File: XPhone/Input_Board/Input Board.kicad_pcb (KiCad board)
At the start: 2 copper layers, 100 x 100 mm, 94 parts, among them J1 AUDIO, J10 ENV, J11 PULSE, J12 PULSE, J13 Power In, J14 Power Out, J2 AUDIO, J3 ENV, J4 ENV, J5 PULSE, J6 PULSE, J7 AUDIO, J8 AUDIO, J9 ENV, Q1 BC847CW, Q2 BC847CW, Q3 BC847CW, Q4 BC847CW, Q5 BC847CW, Q6 BC847CW, Q7 BC847CW, Q8 BC847CW, U1 LM833, U2 78L05, U3 TL084, U4 74HC14, U5 LM833

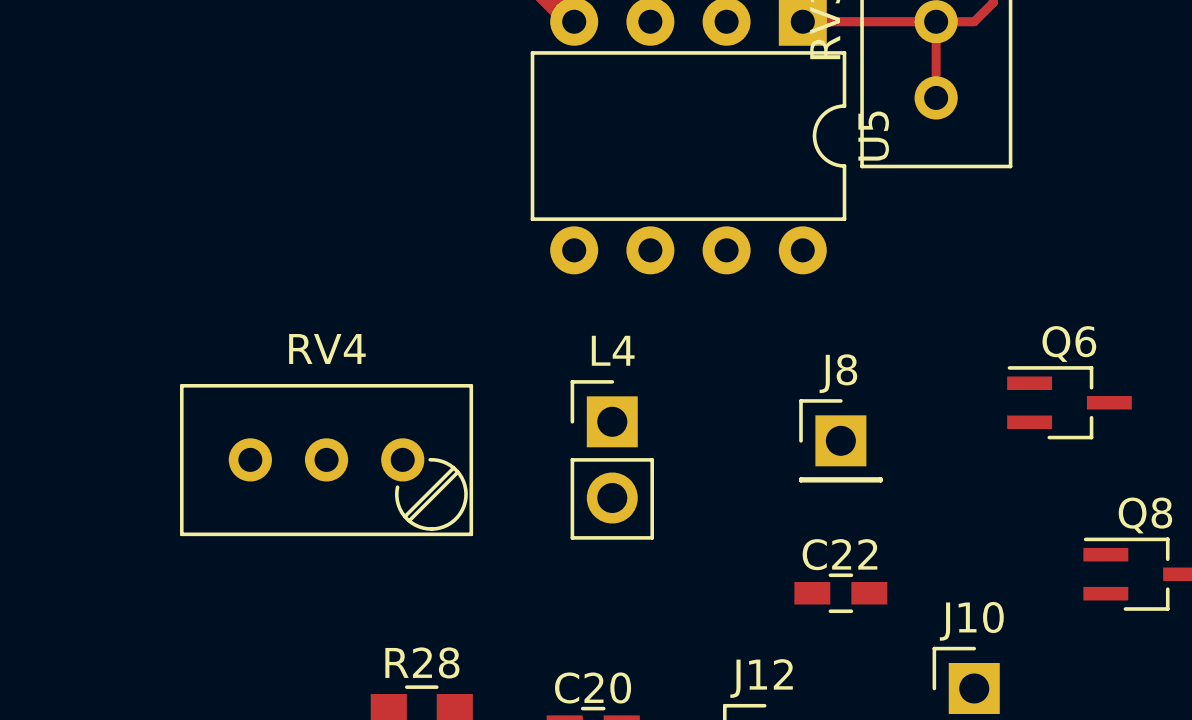
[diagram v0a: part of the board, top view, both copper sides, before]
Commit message: fixed -12V symbol (used to have +12V pin name which automatically connected it with the +12 V supply. BAD. Updated XPhone/Input_Board too
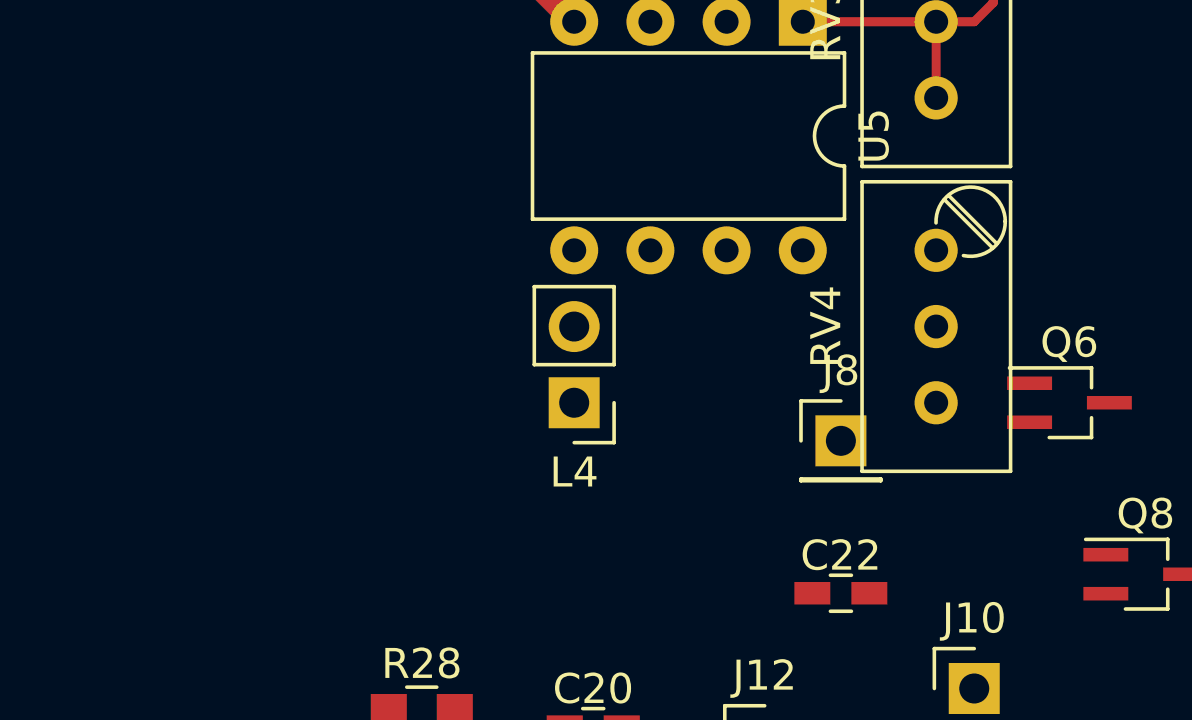
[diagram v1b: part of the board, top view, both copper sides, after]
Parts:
- moved RV4 19.1 mm to (97.8, 63.5), turned to 90 degrees
- moved L4 1.42 mm to (85.7, 68.6), turned to 180 degrees
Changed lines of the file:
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@@
     (links 174)
     (no_connects 146)
-    (area 10.719999 10.719999 111.315 113.11)
+    (area 10.719999 10.719999 110.870001 113.11)
     (thickness 1.6)
     (drawings 4)
@@
     (pad_to_mask_clearance 0.2)
     (aux_axis_origin 0 0)
-    (visible_elements 7FFEF7FF)
+    (visible_elements 7FFEFFFF)
     (pcbplotparams
       (layerselection 0x00000_00000001)
@@
   )
   (module Pin_Headers:Pin_Header_Straight_1x02_Pitch2.54mm (layer F.Cu)
-    (at 86.995 69.215)
+    (at 85.725 68.58 180)
     (descr "Through hole straight pin header, 1x02, 2.54mm pitch, single row")
     (tags "Through hole pin header THT 1x02 2.54mm single row")
-    (fp_text reference L4 (at 0 -2.33) (layer F.SilkS)
+    (fp_text reference L4 (at 0 -2.33 180) (layer F.SilkS)
       (effects (font (size 1 1) (thickness 0.15)))
     )
-    (fp_text value "Input Coil" (at 0 4.87) (layer F.Fab)
+    (fp_text value "Input Coil" (at 0 4.87 180) (layer F.Fab)
       (effects (font (size 1 1) (thickness 0.15)))
     )
@@
     (fp_line (start 1.8 4.35) (end 1.8 -1.8) (layer F.CrtYd) (width 0.05))
     (fp_line (start 1.8 -1.8) (end -1.8 -1.8) (layer F.CrtYd) (width 0.05))
-    (fp_text user %R (at 0 -2.33) (layer F.Fab)
+    (fp_text user %R (at 0 -2.33 180) (layer F.Fab)
       (effects (font (size 1 1) (thickness 0.15)))
     )
-    (pad 1 thru_hole rect (at 0 0) (size 1.7 1.7) (drill 1) (layers *.Cu *.Mask)
+    (pad 1 thru_hole rect (at 0 0 180) (size 1.7 1.7) (drill 1) (layers *.Cu *.Mask)
       (net 3 GNDA))
-    (pad 2 thru_hole oval (at 0 2.54) (size 1.7 1.7) (drill 1) (layers *.Cu *.Mask)
+    (pad 2 thru_hole oval (at 0 2.54 180) (size 1.7 1.7) (drill 1) (layers *.Cu *.Mask)
       (net 16 "Net-(C20-Pad1)"))
     (model ${KISYS3DMOD}/Pin_Headers.3dshapes/Pin_Header_Straight_1x02_Pitch2.54mm.wrl
@@
   )
   (module Potentiometers:Potentiometer_Trimmer_Bourns_3296W (layer F.Cu)
-    (at 80.01 70.485)
+    (at 97.79 63.5 90)
     (descr "Spindle Trimmer Potentiometer, Bourns 3296W, https://www.bourns.com/pdfs/3296.pdf")
     (tags "Spindle Trimmer Potentiometer   Bourns 3296W")
-    (fp_text reference RV4 (at -2.54 -3.66) (layer F.SilkS)
+    (fp_text reference RV4 (at -2.54 -3.66 90) (layer F.SilkS)
       (effects (font (size 1 1) (thickness 0.15)))
     )
-    (fp_text value 10k (at -2.54 3.67) (layer F.Fab)
+    (fp_text value 10k (at -2.54 3.67 90) (layer F.Fab)
       (effects (font (size 1 1) (thickness 0.15)))
     )
@@
     (fp_line (start 2.5 2.7) (end 2.5 -2.7) (layer F.CrtYd) (width 0.05))
     (fp_line (start 2.5 -2.7) (end -7.6 -2.7) (layer F.CrtYd) (width 0.05))
-    (pad 1 thru_hole circle (at 0 0) (size 1.44 1.44) (drill 0.8) (layers *.Cu *.Mask)
+    (pad 1 thru_hole circle (at 0 0 90) (size 1.44 1.44) (drill 0.8) (layers *.Cu *.Mask)
       (net 20 "Net-(C22-Pad2)"))
-    (pad 2 thru_hole circle (at -2.54 0) (size 1.44 1.44) (drill 0.8) (layers *.Cu *.Mask)
+    (pad 2 thru_hole circle (at -2.54 0 90) (size 1.44 1.44) (drill 0.8) (layers *.Cu *.Mask)
       (net 19 "Net-(C22-Pad1)"))
-    (pad 3 thru_hole circle (at -5.08 0) (size 1.44 1.44) (drill 0.8) (layers *.Cu *.Mask)
+    (pad 3 thru_hole circle (at -5.08 0 90) (size 1.44 1.44) (drill 0.8) (layers *.Cu *.Mask)
       (net 19 "Net-(C22-Pad1)"))
     (model Potentiometers.3dshapes/Potentiometer_Trimmer_Bourns_3296W.wrl
@@
   (gr_line (start 110.795 10.795) (end 110.795 110.795) (angle 90) (layer Edge.Cuts) (width 0.15))
   (gr_line (start 10.795 10.795) (end 110.795 10.795) (angle 90) (layer Edge.Cuts) (width 0.15))
-  (segment (start 85.725 55.88) (end 84.455 54.61) (width 0.8) (layer F.Cu) (net 1) (status 400000))
-  (segment (start 84.455 54.61) (end 84.455 53.17) (width 0.8) (layer F.Cu) (net 1) (status 800000))
-  (segment (start 91.125 48.26) (end 91.125 50.02) (width 0.8) (layer F.Cu) (net 3) (status C00000))
-  (segment (start 91.125 50.02) (end 91.44 50.335) (width 0.8) (layer F.Cu) (net 3) (status C00000))
+  (segment (start 85.725 55.88) (end 84.455 54.61) (width 0.8) (layer F.Cu) (net 1))
+  (segment (start 84.455 54.61) (end 84.455 53.17) (width 0.8) (layer F.Cu) (net 1))
+  (segment (start 91.125 48.26) (end 91.125 50.02) (width 0.8) (layer F.Cu) (net 3))
+  (segment (start 91.125 50.02) (end 91.44 50.335) (width 0.8) (layer F.Cu) (net 3))
   (segment (start 87.01 45.78) (end 87.055 45.78) (width 0.8) (layer F.Cu) (net 3))
   (segment (start 87.055 45.78) (end 87.63 46.355) (width 0.8) (layer F.Cu) (net 3))
@@
   (segment (start 91.44 53.975) (end 91.44 52.535) (width 0.3) (layer F.Cu) (net 18))
   (segment (start 90.805 54.61) (end 91.44 53.975) (width 0.3) (layer F.Cu) (net 18))
-  (segment (start 93.175 46.355) (end 93.175 45.235) (width 0.3) (layer F.Cu) (net 21) (status C00000))
-  (segment (start 93.175 45.235) (end 93.025 45.085) (width 0.3) (layer F.Cu) (net 21) (status C00000))
-  (segment (start 93.175 46.355) (end 95.25 46.355) (width 0.3) (layer F.Cu) (net 21) (status C00000))
-  (segment (start 95.25 46.355) (end 95.25 46.93) (width 0.3) (layer F.Cu) (net 21) (status C00000))
+  (segment (start 93.175 46.355) (end 93.175 45.235) (width 0.3) (layer F.Cu) (net 21))
+  (segment (start 93.175 45.235) (end 93.025 45.085) (width 0.3) (layer F.Cu) (net 21))
+  (segment (start 93.175 46.355) (end 95.25 46.355) (width 0.3) (layer F.Cu) (net 21))
+  (segment (start 95.25 46.355) (end 95.25 46.93) (width 0.3) (layer F.Cu) (net 21))
   (segment (start 93.175 46.355) (end 93.175 48.11) (width 0.3) (layer F.Cu) (net 21) (status 10))
   (segment (start 93.175 48.11) (end 93.025 48.26) (width 0.3) (layer F.Cu) (net 21))
   (segment (start 93.235 46.295) (end 93.175 46.355) (width 0.3) (layer F.Cu) (net 21) (status 30))
-  (segment (start 91.125 45.085) (end 89.535 45.085) (width 0.3) (layer F.Cu) (net 23) (status 400000))
-  (segment (start 89.535 45.085) (end 89.535 45.89) (width 0.3) (layer F.Cu) (net 23) (status 800000))
+  (segment (start 91.125 45.085) (end 89.535 45.085) (width 0.3) (layer F.Cu) (net 23))
+  (segment (start 89.535 45.085) (end 89.535 45.89) (width 0.3) (layer F.Cu) (net 23))
   (segment (start 98.425 46.99) (end 98.425 47.625) (width 0.3) (layer F.Cu) (net 31))
   (segment (start 98.425 47.625) (end 98.89 48.09) (width 0.3) (layer F.Cu) (net 31))
   (segment (start 98.89 48.09) (end 98.89 49.53) (width 0.3) (layer F.Cu) (net 31))
-  (via (at 90.975 46.355) (size 1) (drill 0.6) (layers F.Cu B.Cu) (net 37) (status C00000))
-  (segment (start 90.975 46.355) (end 90.805 46.355) (width 0.3) (layer B.Cu) (net 37) (status 400000))
+  (via (at 90.975 46.355) (size 1) (drill 0.6) (layers F.Cu B.Cu) (net 37))
+  (segment (start 90.975 46.355) (end 90.805 46.355) (width 0.3) (layer B.Cu) (net 37))
   (segment (start 85.71 45.78) (end 84.685 45.78) (width 0.3) (layer F.Cu) (net 44))
   (segment (start 84.685 45.78) (end 84.455 45.55) (width 0.3) (layer F.Cu) (net 44))
@@
   (segment (start 89.535 48.895) (end 84.455 48.895) (width 0.3) (layer B.Cu) (net 44))
   (via (at 89.535 48.895) (size 1) (drill 0.6) (layers F.Cu B.Cu) (net 44))
-  (segment (start 84.455 50.97) (end 84.455 48.895) (width 0.3) (layer F.Cu) (net 46) (status 400000))
+  (segment (start 84.455 50.97) (end 84.455 48.895) (width 0.3) (layer F.Cu) (net 46))
   (segment (start 83.185 42.545) (end 84.455 42.545) (width 0.3) (layer F.Cu) (net 46))
   (segment (start 83.185 47.625) (end 83.185 42.545) (width 0.3) (layer F.Cu) (net 46))

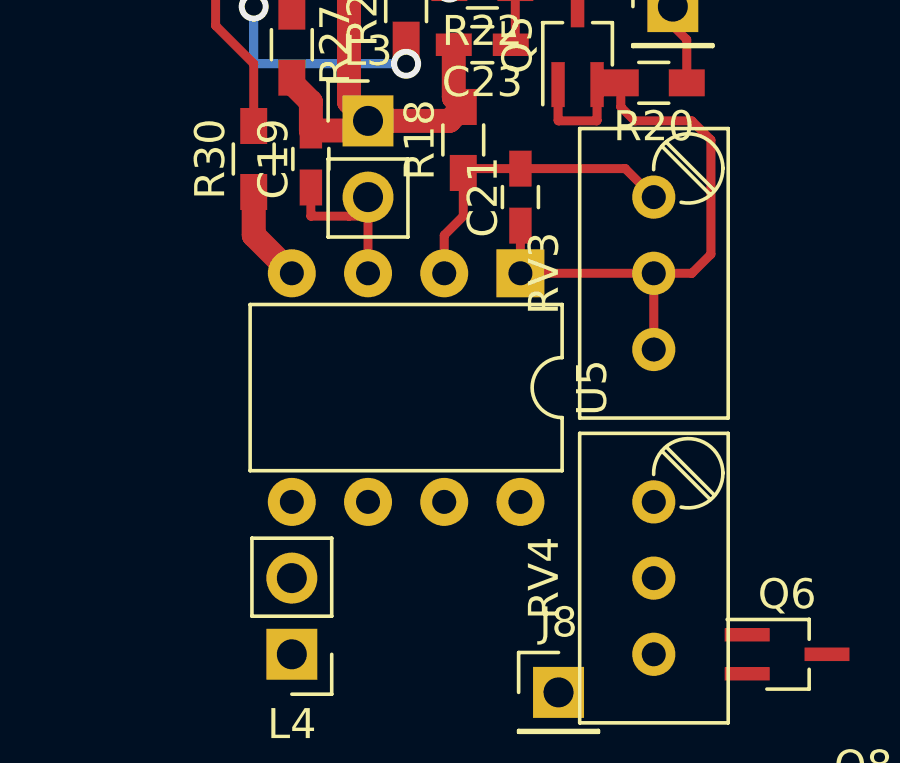
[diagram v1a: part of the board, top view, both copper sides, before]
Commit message: XPhone/Input_Board - fixed bug - +12V and -12V were the same net. Not any more
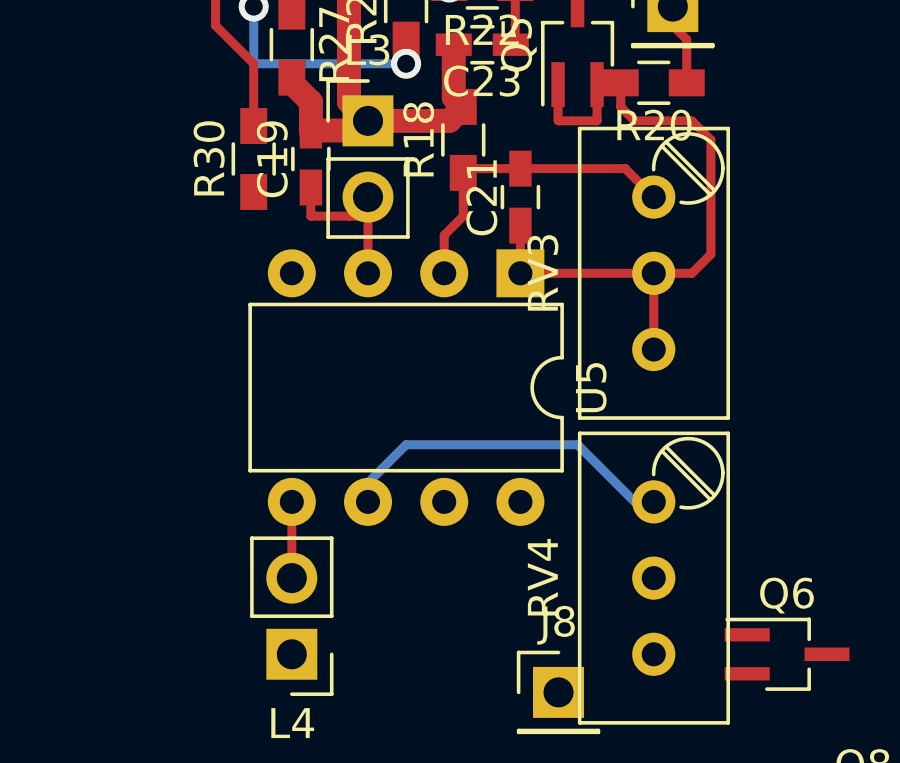
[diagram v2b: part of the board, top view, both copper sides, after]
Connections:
- C1 pad 2: +12V -> -12V
- C10 pad 2: +12V -> -12V
- C12 pad 2: +12V -> -12V
- C2 pad 2: +12V -> -12V
- C5 pad 2: +12V -> -12V
- C6 pad 2: +12V -> -12V
- C9 pad 2: +12V -> -12V
- J13 pad 3: +12V -> -12V
- J14 pad 3: +12V -> -12V
- U1 pad 4: +12V -> -12V
- U3 pad 11: +12V -> -12V
- U4 pad 10: Net-(U4-Pad10) -> (no net)
- U4 pad 11: Net-(U4-Pad11) -> (no net)
- U4 pad 12: Net-(U4-Pad12) -> (no net)
- U4 pad 13: Net-(U4-Pad13) -> (no net)
- U5 pad 4: +12V -> -12V
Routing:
- net Net-(C22-Pad2): track 0.00 -> 11.5 mm
- net +12V: track 3.24 -> 0.00 mm
- net Net-(C20-Pad1): track 0.00 -> 2.54 mm
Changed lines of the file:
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@@
 (kicad_pcb (version 4) (host pcbnew 4.0.6)
   (general
-    (links 174)
-    (no_connects 146)
-    (area 10.719999 10.719999 110.870001 113.11)
+    (links 173)
+    (no_connects 144)
+    (area 10.719999 10.719999 110.870001 110.870001)
     (thickness 1.6)
     (drawings 4)
-    (tracks 77)
+    (tracks 81)
     (zones 0)
     (modules 94)
-    (nets 54)
+    (nets 51)
   )
   (page A4)
@@
   (net 48 "Net-(R32-Pad1)")
   (net 49 "Net-(R33-Pad1)")
-  (net 50 "Net-(U4-Pad10)")
-  (net 51 "Net-(U4-Pad11)")
-  (net 52 "Net-(U4-Pad12)")
-  (net 53 "Net-(U4-Pad13)")
+  (net 50 -12V)
   (net_class Default "This is the default net class."
     (clearance 0.3)
@@
     (uvia_dia 0.3)
     (uvia_drill 0.1)
+    (add_net -12V)
     (add_net "Net-(C13-Pad1)")
     (add_net "Net-(C14-Pad1)")
@@
     (add_net "Net-(R32-Pad1)")
     (add_net "Net-(R33-Pad1)")
-    (add_net "Net-(U4-Pad10)")
-    (add_net "Net-(U4-Pad11)")
-    (add_net "Net-(U4-Pad12)")
-    (add_net "Net-(U4-Pad13)")
     (add_net V_ENV_BIAS)
   )
@@
     (pad 3 thru_hole oval (at 0 5.08) (size 1.6 1.6) (drill 0.8) (layers *.Cu *.Mask)
       (net 43 "Net-(R17-Pad1)"))
-    (pad 10 thru_hole oval (at 7.62 10.16) (size 1.6 1.6) (drill 0.8) (layers *.Cu *.Mask)
-      (net 50 "Net-(U4-Pad10)"))
+    (pad 10 thru_hole oval (at 7.62 10.16) (size 1.6 1.6) (drill 0.8) (layers *.Cu *.Mask))
     (pad 4 thru_hole oval (at 0 7.62) (size 1.6 1.6) (drill 0.8) (layers *.Cu *.Mask)
       (net 30 "Net-(J6-Pad1)"))
-    (pad 11 thru_hole oval (at 7.62 7.62) (size 1.6 1.6) (drill 0.8) (layers *.Cu *.Mask)
-      (net 51 "Net-(U4-Pad11)"))
+    (pad 11 thru_hole oval (at 7.62 7.62) (size 1.6 1.6) (drill 0.8) (layers *.Cu *.Mask))
     (pad 5 thru_hole oval (at 0 10.16) (size 1.6 1.6) (drill 0.8) (layers *.Cu *.Mask)
       (net 48 "Net-(R32-Pad1)"))
-    (pad 12 thru_hole oval (at 7.62 5.08) (size 1.6 1.6) (drill 0.8) (layers *.Cu *.Mask)
-      (net 52 "Net-(U4-Pad12)"))
+    (pad 12 thru_hole oval (at 7.62 5.08) (size 1.6 1.6) (drill 0.8) (layers *.Cu *.Mask))
     (pad 6 thru_hole oval (at 0 12.7) (size 1.6 1.6) (drill 0.8) (layers *.Cu *.Mask)
       (net 35 "Net-(J11-Pad1)"))
-    (pad 13 thru_hole oval (at 7.62 2.54) (size 1.6 1.6) (drill 0.8) (layers *.Cu *.Mask)
-      (net 53 "Net-(U4-Pad13)"))
+    (pad 13 thru_hole oval (at 7.62 2.54) (size 1.6 1.6) (drill 0.8) (layers *.Cu *.Mask))
     (pad 7 thru_hole oval (at 0 15.24) (size 1.6 1.6) (drill 0.8) (layers *.Cu *.Mask)
       (net 9 GND))
@@
       (net 7 "Net-(C8-Pad1)"))
     (pad 4 thru_hole oval (at 0 7.62 270) (size 1.6 1.6) (drill 0.8) (layers *.Cu *.Mask)
-      (net 1 +12V))
+      (net 50 -12V))
     (pad 8 thru_hole oval (at 7.62 0 270) (size 1.6 1.6) (drill 0.8) (layers *.Cu *.Mask)
       (net 1 +12V))
@@
       (net 19 "Net-(C22-Pad1)"))
     (pad 4 thru_hole oval (at 0 7.62 270) (size 1.6 1.6) (drill 0.8) (layers *.Cu *.Mask)
-      (net 1 +12V))
+      (net 50 -12V))
     (pad 8 thru_hole oval (at 7.62 0 270) (size 1.6 1.6) (drill 0.8) (layers *.Cu *.Mask)
       (net 1 +12V))
@@
       (net 9 GND))
     (pad 3 thru_hole oval (at 0 5.08 90) (size 1.7 1.7) (drill 1) (layers *.Cu *.Mask)
-      (net 1 +12V))
+      (net 50 -12V))
     (model ${KISYS3DMOD}/Pin_Headers.3dshapes/Pin_Header_Straight_1x03_Pitch2.54mm.wrl
       (at (xyz 0 -0.1 0))
@@
       (net 9 GND))
     (pad 3 thru_hole oval (at 0 5.08 90) (size 1.7 1.7) (drill 1) (layers *.Cu *.Mask)
-      (net 1 +12V))
+      (net 50 -12V))
     (model ${KISYS3DMOD}/Pin_Headers.3dshapes/Pin_Header_Straight_1x03_Pitch2.54mm.wrl
       (at (xyz 0 -0.1 0))
@@
       (net 9 GND))
     (pad 2 smd rect (at 0.95 0) (size 1.2 0.75) (layers F.Cu F.Paste F.Mask)
-      (net 1 +12V))
+      (net 50 -12V))
     (model Capacitors_SMD.3dshapes/C_0603.wrl
       (at (xyz 0 0 0))
@@
       (net 1 +12V))
     (pad 2 smd rect (at 0.95 0) (size 1.2 0.75) (layers F.Cu F.Paste F.Mask)
-      (net 1 +12V))
+      (net 50 -12V))
     (model Capacitors_SMD.3dshapes/C_0603.wrl
       (at (xyz 0 0 0))
@@
       (net 1 +12V))
     (pad 2 smd rect (at 0.95 0) (size 1.2 0.75) (layers F.Cu F.Paste F.Mask)
-      (net 1 +12V))
+      (net 50 -12V))
     (model Capacitors_SMD.3dshapes/C_0603.wrl
       (at (xyz 0 0 0))
@@
       (net 1 +12V))
     (pad 2 smd rect (at 0.95 0) (size 1.2 0.75) (layers F.Cu F.Paste F.Mask)
-      (net 1 +12V))
+      (net 50 -12V))
     (model Capacitors_SMD.3dshapes/C_0603.wrl
       (at (xyz 0 0 0))
@@
       (net 1 +12V))
     (pad 2 smd rect (at 0.95 0) (size 1.2 0.75) (layers F.Cu F.Paste F.Mask)
-      (net 1 +12V))
+      (net 50 -12V))
     (model Capacitors_SMD.3dshapes/C_0603.wrl
       (at (xyz 0 0 0))
@@
       (net 1 +12V))
     (pad 2 smd rect (at 0.95 0) (size 1.2 0.75) (layers F.Cu F.Paste F.Mask)
-      (net 1 +12V))
+      (net 50 -12V))
     (model Capacitors_SMD.3dshapes/C_0603.wrl
       (at (xyz 0 0 0))
@@
       (net 1 +12V))
     (pad 2 smd rect (at 0.95 0) (size 1.2 0.75) (layers F.Cu F.Paste F.Mask)
-      (net 1 +12V))
+      (net 50 -12V))
     (model Capacitors_SMD.3dshapes/C_0603.wrl
       (at (xyz 0 0 0))
@@
       (net 33 "Net-(J9-Pad1)"))
     (pad 11 smd rect (at 0 -3.048) (size 0.508 1.143) (layers F.Cu F.Paste F.Mask)
-      (net 1 +12V))
+      (net 50 -12V))
     (pad 12 smd rect (at -1.27 -3.048) (size 0.508 1.143) (layers F.Cu F.Paste F.Mask)
       (net 22 "Net-(C24-Pad1)"))
@@
   (gr_line (start 110.795 10.795) (end 110.795 110.795) (angle 90) (layer Edge.Cuts) (width 0.15))
   (gr_line (start 10.795 10.795) (end 110.795 10.795) (angle 90) (layer Edge.Cuts) (width 0.15))
-  (segment (start 85.725 55.88) (end 84.455 54.61) (width 0.8) (layer F.Cu) (net 1))
-  (segment (start 84.455 54.61) (end 84.455 53.17) (width 0.8) (layer F.Cu) (net 1))
   (segment (start 91.125 48.26) (end 91.125 50.02) (width 0.8) (layer F.Cu) (net 3))
   (segment (start 91.125 50.02) (end 91.44 50.335) (width 0.8) (layer F.Cu) (net 3))
@@
   (segment (start 88.265 53.975) (end 88.265 53.34) (width 0.3) (layer F.Cu) (net 15))
   (segment (start 88.265 55.88) (end 88.265 53.34) (width 0.3) (layer F.Cu) (net 15))
+  (segment (start 85.725 63.5) (end 85.725 66.04) (width 0.3) (layer F.Cu) (net 16) (status C00000))
   (segment (start 96.69 49.53) (end 96.69 50.335) (width 0.3) (layer F.Cu) (net 17))
   (segment (start 99.06 55.88) (end 97.79 55.88) (width 0.3) (layer F.Cu) (net 17))
@@
   (segment (start 91.44 53.975) (end 91.44 52.535) (width 0.3) (layer F.Cu) (net 18))
   (segment (start 90.805 54.61) (end 91.44 53.975) (width 0.3) (layer F.Cu) (net 18))
+  (segment (start 97.79 63.5) (end 97.155 63.5) (width 0.3) (layer B.Cu) (net 20))
+  (segment (start 97.155 63.5) (end 95.25 61.595) (width 0.3) (layer B.Cu) (net 20))
+  (segment (start 95.25 61.595) (end 89.535 61.595) (width 0.3) (layer B.Cu) (net 20))
+  (segment (start 89.535 61.595) (end 88.265 62.865) (width 0.3) (layer B.Cu) (net 20))
+  (segment (start 88.265 62.865) (end 88.265 63.5) (width 0.3) (layer B.Cu) (net 20))
   (segment (start 93.175 46.355) (end 93.175 45.235) (width 0.3) (layer F.Cu) (net 21))
   (segment (start 93.175 45.235) (end 93.025 45.085) (width 0.3) (layer F.Cu) (net 21))
